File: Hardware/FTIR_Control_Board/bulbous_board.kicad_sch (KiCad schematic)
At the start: 37 parts, among them J1 RJ45_LED_Shielded, Q1 NMOS, U1 TSR_1-2450, U2 Peensy4.1_DEV-16771, U3 TMC2208, U4 ADA4610-1xRJ

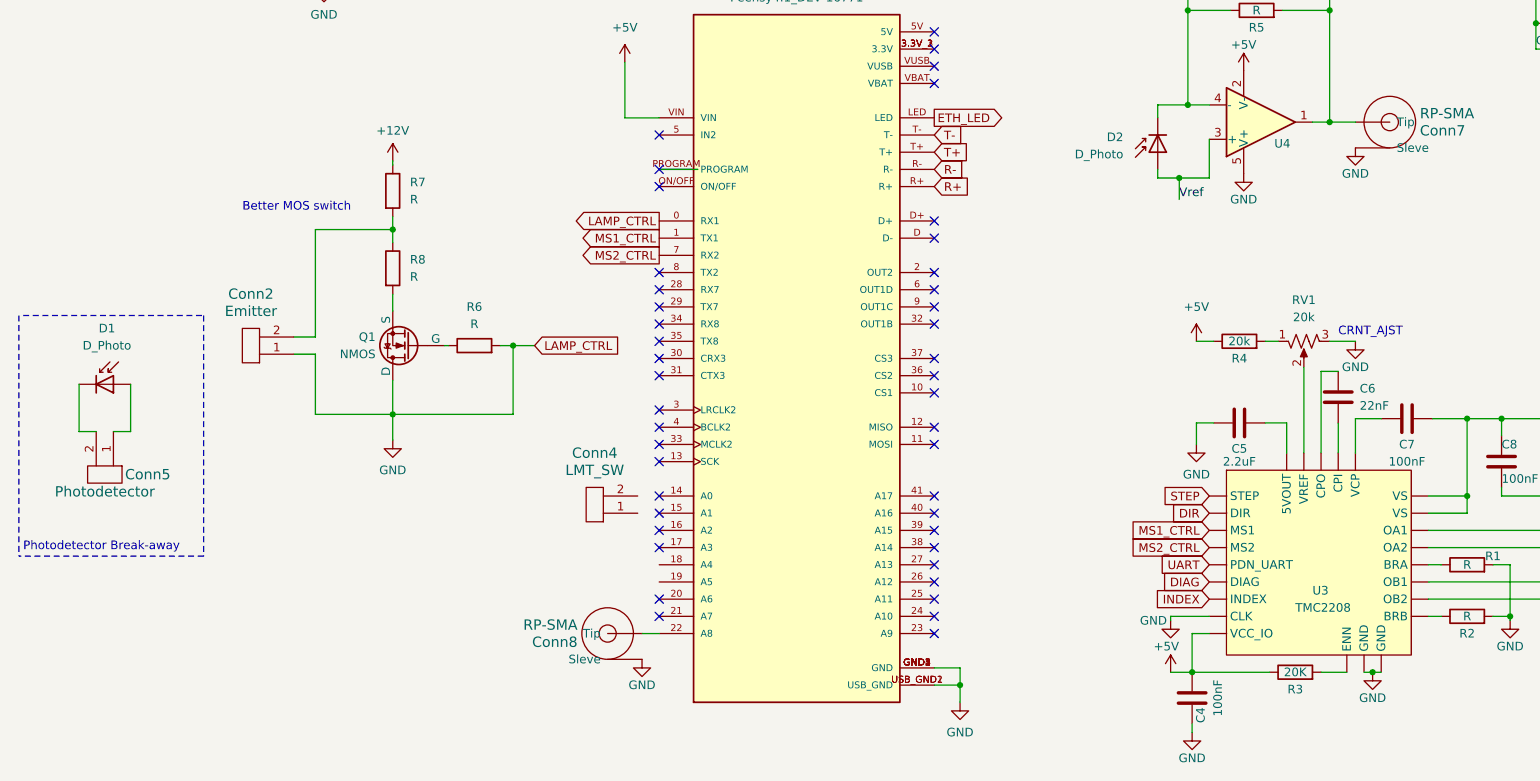
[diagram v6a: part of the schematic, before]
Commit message: Made MOSFET work
It was bad good thing Drew is here
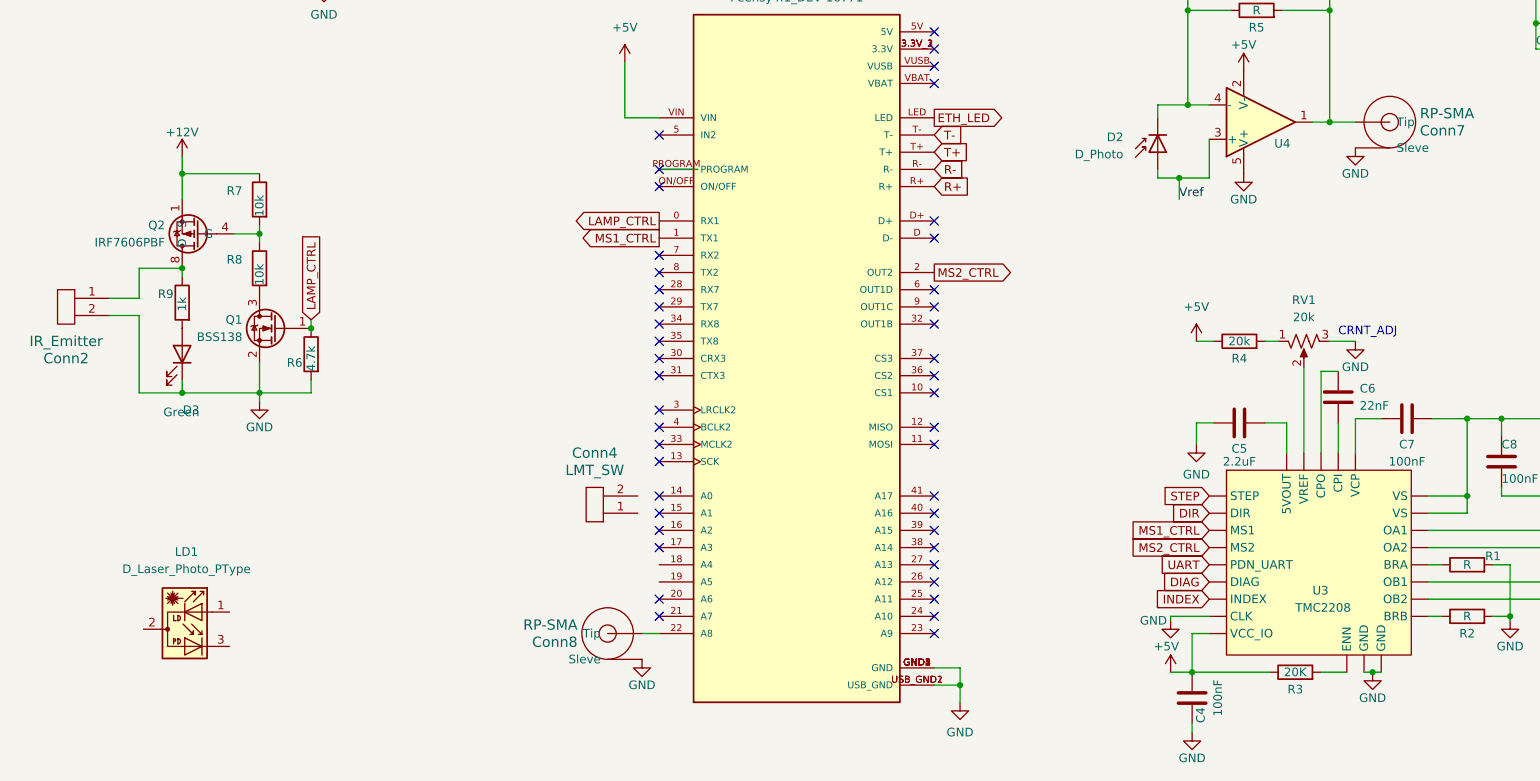
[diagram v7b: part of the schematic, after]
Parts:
- removed Conn5: Photodetector, symbol MRDT_Connectors:Molex_SL_02
- removed D1: D_Photo, symbol Device:D_Photo
- removed Q1: NMOS, symbol Simulation_SPICE:NMOS
- added D3: Green, LED_SMD:LED_0603_1608Metric_Pad1.05x0.95mm_HandSolder, symbol Device:LED
- added LD1: D_Laser_Photo_PType, symbol Device:D_Laser_Photo_PType
- added Q1: BSS138, Package_TO_SOT_SMD:SOT-23, symbol Transistor_FET:BSS138
- added Q2: IRF7606PBF, Package_SO:SOP-8_3.9x4.9mm_P1.27mm, symbol Transistor_FET:IRF7606PBF
- added R9: 1k, Resistor_SMD:R_0603_1608Metric_Pad0.98x0.95mm_HandSolder, symbol Device:R
- Conn2: value Emitter -> IR_Emitter
- R6: value R -> 4.7k; footprint (none) -> Resistor_SMD:R_0603_1608Metric_Pad0.98x0.95mm_HandSolder
- R7, R8: value R -> 10k; footprint (none) -> Resistor_SMD:R_0603_1608Metric_Pad0.98x0.95mm_HandSolder
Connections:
- net +12V: now also Q2.1 (S), Q2.2 (S), Q2.3 (S)
- net GND: now also Conn2.2, D3.1 (K), Q1.2 (S); no longer Conn2.1, U2.0 (RX1)
- net MS2_CTRL: now also U2.2 (OUT2); no longer U2.7 (RX2)
- net at R7.2, R8.1: now also Q2.4 (G); no longer Conn2.2
- net LAMP_CTRL: now reaches R6.1
- net LAMP_CTRL: now also U2.0 (RX1), Q1.1 (G)
- net at R8.2: now also Q1.3 (D)
- new net: Conn2.1, Q2.5 (D), Q2.6 (D), Q2.7 (D), Q2.8 (D), R9.1
- new net: D3.2 (A), R9.2
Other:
- note added: "CRNT_ADJ"
- note removed: "Better MOS switch"
- note removed: "CRNT_AJST"
- note removed: "Photodetector Break-away"

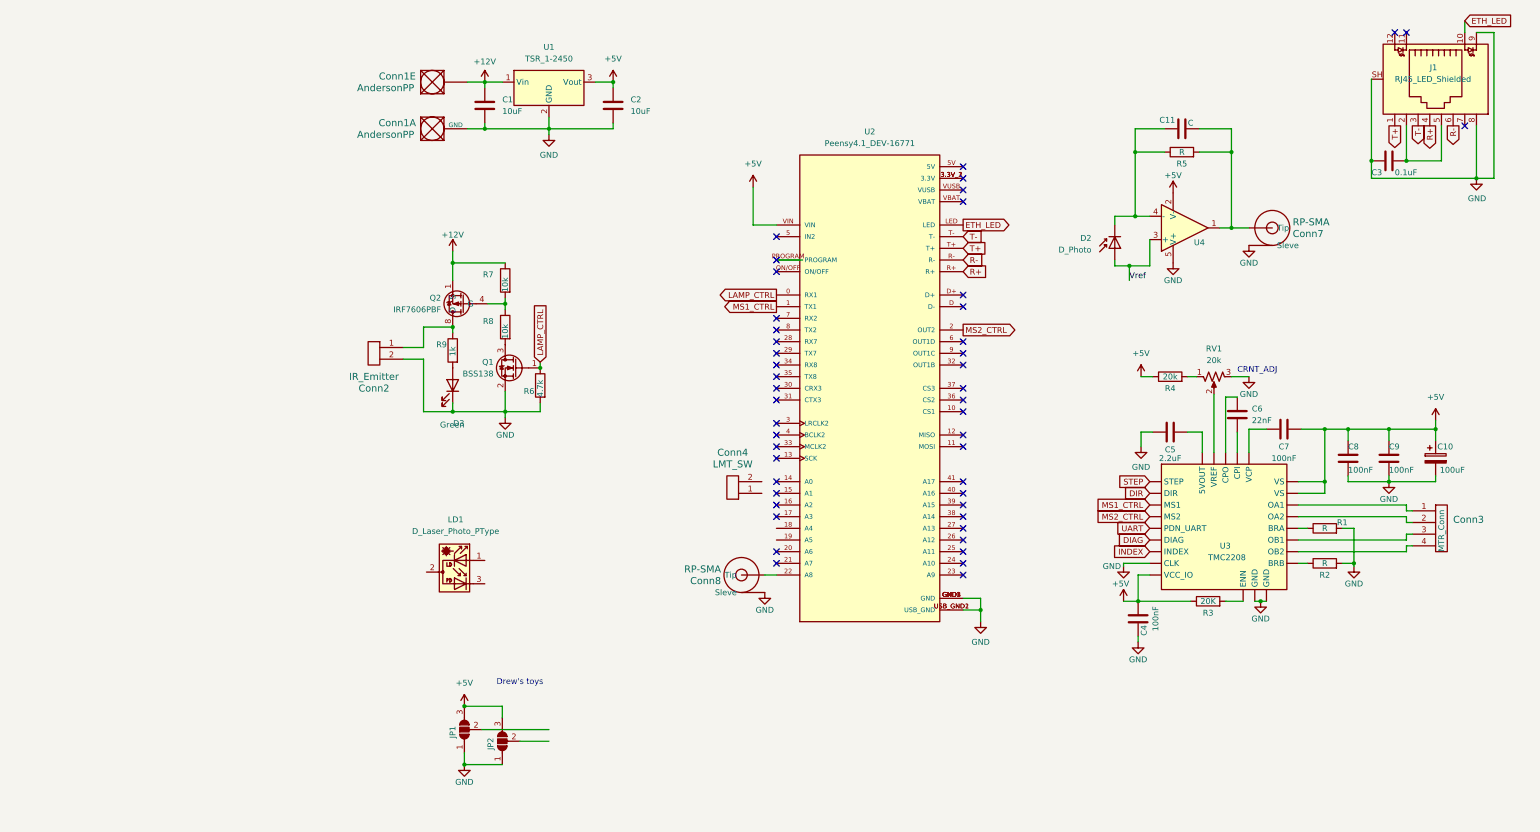
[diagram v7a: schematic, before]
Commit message: Added laser diode driver
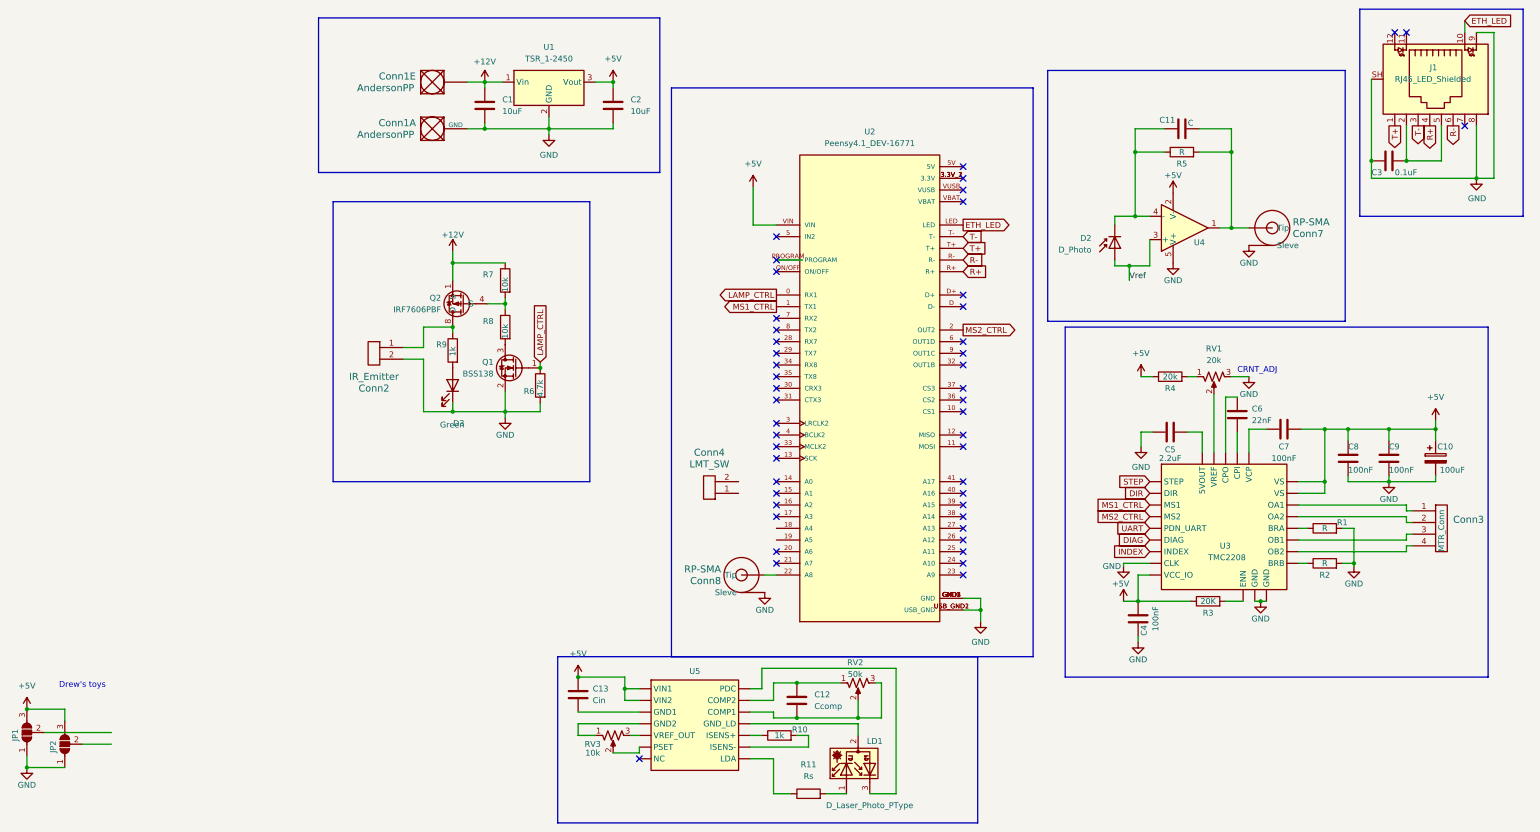
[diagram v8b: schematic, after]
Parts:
- added C12: Ccomp, symbol Device:C
- added C13: Cin, symbol Device:C
- added R10: 1k, symbol Device:R
- added R11: Rs, symbol Device:R
- added RV2: 50k, symbol Device:R_Potentiometer_US
- added RV3: 10k, symbol Device:R_Potentiometer_US
- added U5: ~, symbol MRDT_Devices:MLD203P2
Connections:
- net +5V: now also C13.1, U5. (VREF_OUT)
- net at LD1.1: now also R11.2
- net at LD1.2: now also U5. (VREF_OUT)
- net at LD1.3: now also U5. (VREF_OUT)
- new net: C12.1, RV2.2, RV2.3, U5. (VREF_OUT)
- new net: C12.2, RV2.1, U5. (VREF_OUT)
- new net: RV3.1, U5. (VREF_OUT)
- new net: RV3.2, U5. (VREF_OUT)
- new net: RV3.3, U5. (VREF_OUT)
- new net: R11.1, U5. (VREF_OUT)
- new net: R10.1, U5. (VREF_OUT)
- new net: R10.2, U5. (VREF_OUT)
- new net: C13.2, U5. (VREF_OUT)
- no-connect marks 47 -> 48
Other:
- moved on the sheet: Conn4, JP1, JP2, LD1
